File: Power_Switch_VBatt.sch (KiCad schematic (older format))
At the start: 11 parts

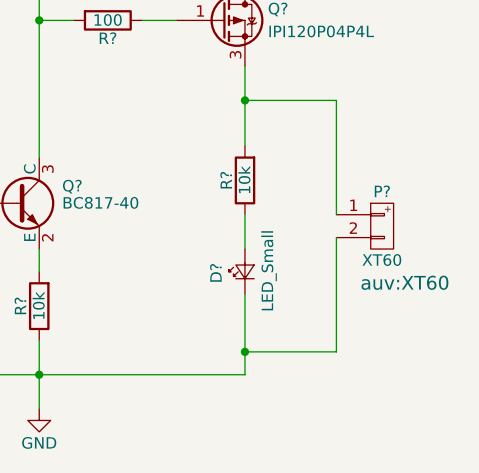
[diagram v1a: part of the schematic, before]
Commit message: Correct all foot-print assignments
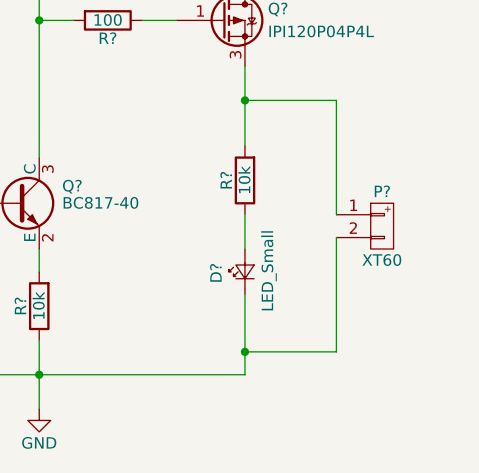
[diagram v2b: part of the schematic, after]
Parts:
- P?: footprint auv:XT60 -> zeabus:XT60
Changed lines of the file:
@@
 $Descr A4 11693 8268
 encoding utf-8
-Sheet 7 12
+Sheet 7 13
 Title ""
 Date ""
@@
 F 0 "P?" H 7050 4350 50  0000 C CNN
 F 1 "XT60" H 7050 4050 50  0000 C CNN
-F 2 "auv:XT60" H 7150 3950 60  0000 C CNN
+F 2 "zeabus:XT60" H 7150 3950 60  0001 C CNN
 F 3 "" H 7050 4200 60  0000 C CNN
 	1    7050 4200

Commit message: Annotate all components
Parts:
- gave numbers to parts that had none: 11
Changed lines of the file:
@@
 LIBS:zeabus
 LIBS:ftdi
-LIBS:Power_Distributor-cache
 EELAYER 25 0
 EELAYER END
 $Descr A4 11693 8268
 encoding utf-8
-Sheet 7 13
+Sheet 8 13
 Title ""
 Date ""
@@
 $EndDescr
 $Comp
-L Q_PMOS_GDS Q?
+L Q_PMOS_GDS Q6
 U 1 1 58E52089
 P 6350 3300
-AR Path="/58E527AF/58E52089" Ref="Q?"  Part="1"
-AR Path="/58E51F99/58E52089" Ref="Q?"  Part="1"
-F 0 "Q?" H 6550 3350 50  0000 L CNN
+AR Path="/58E51F99/58E52089" Ref="Q6"  Part="1"
+AR Path="/58E527AF/58E52089" Ref="Q8"  Part="1"
+F 0 "Q8" H 6550 3350 50  0000 L CNN
 F 1 "IPI120P04P4L" H 6550 3250 50  0000 L CNN
 F 2 "TO_SOT_Packages_SMD:TO-263-3Lead" H 6550 3400 50  0001 C CNN
@@
 $EndComp
 $Comp
-L R R?
+L R R16
 U 1 1 58E5219E
 P 5850 3300
-AR Path="/58E527AF/58E5219E" Ref="R?"  Part="1"
-AR Path="/58E51F99/58E5219E" Ref="R?"  Part="1"
-F 0 "R?" V 5930 3300 50  0000 C CNN
+AR Path="/58E51F99/58E5219E" Ref="R16"  Part="1"
+AR Path="/58E527AF/58E5219E" Ref="R21"  Part="1"
+F 0 "R21" V 5930 3300 50  0000 C CNN
 F 1 "100" V 5850 3300 50  0000 C CNN
 F 2 "Resistors_SMD:R_0603" V 5780 3300 50  0001 C CNN
@@
 $EndComp
 $Comp
-L XT60 P?
+L XT60 P12
 U 1 1 58E521F9
 P 7050 4200
-AR Path="/58E527AF/58E521F9" Ref="P?"  Part="1"
-AR Path="/58E51F99/58E521F9" Ref="P?"  Part="1"
-F 0 "P?" H 7050 4350 50  0000 C CNN
+AR Path="/58E51F99/58E521F9" Ref="P12"  Part="1"
+AR Path="/58E527AF/58E521F9" Ref="P13"  Part="1"
+F 0 "P13" H 7050 4350 50  0000 C CNN
 F 1 "XT60" H 7050 4050 50  0000 C CNN
 F 2 "zeabus:XT60" H 7150 3950 60  0001 C CNN
@@
 $EndComp
 $Comp
-L LED_Small D?
+L LED_Small D9
 U 1 1 58E52234
 P 6450 4400
-AR Path="/58E527AF/58E52234" Ref="D?"  Part="1"
-AR Path="/58E51F99/58E52234" Ref="D?"  Part="1"
-F 0 "D?" H 6400 4525 50  0000 L CNN
+AR Path="/58E51F99/58E52234" Ref="D9"  Part="1"
+AR Path="/58E527AF/58E52234" Ref="D11"  Part="1"
+F 0 "D11" H 6400 4525 50  0000 L CNN
 F 1 "LED_Small" H 6275 4300 50  0000 L CNN
 F 2 "LEDs:LED_0603" V 6450 4400 50  0001 C CNN
@@
 $EndComp
 $Comp
-L R R?
+L R R15
 U 1 1 58E5234D
 P 5850 2950
-AR Path="/58E527AF/58E5234D" Ref="R?"  Part="1"
-AR Path="/58E51F99/58E5234D" Ref="R?"  Part="1"
-F 0 "R?" V 5930 2950 50  0000 C CNN
+AR Path="/58E51F99/58E5234D" Ref="R15"  Part="1"
+AR Path="/58E527AF/58E5234D" Ref="R20"  Part="1"
+F 0 "R20" V 5930 2950 50  0000 C CNN
 F 1 "10k" V 5850 2950 50  0000 C CNN
 F 2 "Resistors_SMD:R_0603" V 5780 2950 50  0001 C CNN
@@
 $EndComp
 $Comp
-L R R?
+L R R17
 U 1 1 58E52389
 P 6450 4000
-AR Path="/58E527AF/58E52389" Ref="R?"  Part="1"
-AR Path="/58E51F99/58E52389" Ref="R?"  Part="1"
-F 0 "R?" V 6530 4000 50  0000 C CNN
+AR Path="/58E51F99/58E52389" Ref="R17"  Part="1"
+AR Path="/58E527AF/58E52389" Ref="R22"  Part="1"
+F 0 "R22" V 6530 4000 50  0000 C CNN
 F 1 "10k" V 6450 4000 50  0000 C CNN
 F 2 "Resistors_SMD:R_0603" V 6380 4000 50  0001 C CNN
@@
 $EndComp
 $Comp
-L BC817-40 Q?
+L BC817-40 Q5
 U 1 1 58E52473
 P 5450 4100
-AR Path="/58E527AF/58E52473" Ref="Q?"  Part="1"
-AR Path="/58E51F99/58E52473" Ref="Q?"  Part="1"
-F 0 "Q?" H 5650 4175 50  0000 L CNN
+AR Path="/58E51F99/58E52473" Ref="Q5"  Part="1"
+AR Path="/58E527AF/58E52473" Ref="Q7"  Part="1"
+F 0 "Q7" H 5650 4175 50  0000 L CNN
 F 1 "BC817-40" H 5650 4100 50  0000 L CNN
 F 2 "TO_SOT_Packages_SMD:SOT-23" H 5650 4025 50  0001 L CIN
@@
 $EndComp
 $Comp
-L R R?
+L R R13
 U 1 1 58E526E2
 P 4300 4100
-AR Path="/58E527AF/58E526E2" Ref="R?"  Part="1"
-AR Path="/58E51F99/58E526E2" Ref="R?"  Part="1"
-F 0 "R?" V 4380 4100 50  0000 C CNN
+AR Path="/58E51F99/58E526E2" Ref="R13"  Part="1"
+AR Path="/58E527AF/58E526E2" Ref="R18"  Part="1"
+F 0 "R18" V 4380 4100 50  0000 C CNN
 F 1 "2.2k" V 4300 4100 50  0000 C CNN
 F 2 "Resistors_SMD:R_0603" V 4230 4100 50  0001 C CNN
@@
 $EndComp
 $Comp
-L C C?
+L C C2
 U 1 1 58E5272C
 P 4900 4400
-AR Path="/58E527AF/58E5272C" Ref="C?"  Part="1"
-AR Path="/58E51F99/58E5272C" Ref="C?"  Part="1"
-F 0 "C?" H 4925 4500 50  0000 L CNN
+AR Path="/58E51F99/58E5272C" Ref="C2"  Part="1"
+AR Path="/58E527AF/58E5272C" Ref="C3"  Part="1"
+F 0 "C3" H 4925 4500 50  0000 L CNN
 F 1 "1nF" H 4925 4300 50  0000 L CNN
 F 2 "Capacitors_SMD:C_0603" H 4938 4250 50  0001 C CNN
@@
 $EndComp
 $Comp
-L D D?
+L D D8
 U 1 1 58E5279D
 P 4600 4400
-AR Path="/58E527AF/58E5279D" Ref="D?"  Part="1"
-AR Path="/58E51F99/58E5279D" Ref="D?"  Part="1"
-F 0 "D?" H 4600 4500 50  0000 C CNN
+AR Path="/58E51F99/58E5279D" Ref="D8"  Part="1"
+AR Path="/58E527AF/58E5279D" Ref="D10"  Part="1"
+F 0 "D10" H 4600 4500 50  0000 C CNN
 F 1 "D" H 4600 4300 50  0000 C CNN
 F 2 "Diodes_SMD:D_SOD-123" H 4600 4400 50  0001 C CNN
@@
 $EndComp
 $Comp
-L GND #PWR?
+L GND #PWR021
 U 1 1 58E527F8
 P 5550 5000
-AR Path="/58E527AF/58E527F8" Ref="#PWR?"  Part="1"
-AR Path="/58E51F99/58E527F8" Ref="#PWR?"  Part="1"
-F 0 "#PWR?" H 5550 4750 50  0001 C CNN
+AR Path="/58E51F99/58E527F8" Ref="#PWR021"  Part="1"
+AR Path="/58E527AF/58E527F8" Ref="#PWR022"  Part="1"
+F 0 "#PWR022" H 5550 4750 50  0001 C CNN
 F 1 "GND" H 5550 4850 50  0000 C CNN
 F 2 "" H 5550 5000 50  0001 C CNN
@@
 	6850 4250 6850 4750
 $Comp
-L R R?
+L R R14
 U 1 1 58E6A1DE
 P 5550 4550
-AR Path="/58E51F99/58E6A1DE" Ref="R?"  Part="1"
-AR Path="/58E527AF/58E6A1DE" Ref="R?"  Part="1"
-F 0 "R?" V 5630 4550 50  0000 C CNN
+AR Path="/58E51F99/58E6A1DE" Ref="R14"  Part="1"
+AR Path="/58E527AF/58E6A1DE" Ref="R19"  Part="1"
+F 0 "R19" V 5630 4550 50  0000 C CNN
 F 1 "10k" V 5550 4550 50  0000 C CNN
 F 2 "Resistors_SMD:R_0603" V 5480 4550 50  0001 C CNN

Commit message: Bug fixed and clean-up for PCB generating
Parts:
- removed D8: D, Diodes_SMD:D_SOD-123, symbol D
- added D4: BZX585-C12, Diodes_SMD:SOD-523, symbol D_Zener
- added F2: Fuse, Zeabus:FUSE_AUTO, symbol Fuse
- C2: value 1nF -> 1uF
- Q4: renamed from Q6; value IPI120P04P4L -> IPD90P03P4L; footprint TO_SOT_Packages_SMD:TO-263-3Lead -> TO_SOT_Packages_SMD:TO-252-2Lead
- R9: renamed from R16; value 100 -> 1k
- renumbered D9 to D5, P12 to P5, Q5 to Q3, R17 to R10, R13 to R6, R14 to R7, R15 to R8
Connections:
- net labels removed: Hardware_Switch
- wire segments 24 -> 23
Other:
- moved on the sheet: D7, P6, R13, R15
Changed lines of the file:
@@
 $Descr A4 11693 8268
 encoding utf-8
-Sheet 8 13
+Sheet 3 10
 Title ""
-Date ""
-Rev ""
+Date "2017-04-06"
+Rev "1.0.0"
 Comp ""
 Comment1 ""
@@
 $EndDescr
 $Comp
-L Q_PMOS_GDS Q6
+L Q_PMOS_GDS Q4
 U 1 1 58E52089
 P 6350 3300
-AR Path="/58E51F99/58E52089" Ref="Q6"  Part="1"
-AR Path="/58E527AF/58E52089" Ref="Q8"  Part="1"
-F 0 "Q8" H 6550 3350 50  0000 L CNN
-F 1 "IPI120P04P4L" H 6550 3250 50  0000 L CNN
-F 2 "TO_SOT_Packages_SMD:TO-263-3Lead" H 6550 3400 50  0001 C CNN
+AR Path="/58E51F99/58E52089" Ref="Q4"  Part="1"
+AR Path="/58E527AF/58E52089" Ref="Q6"  Part="1"
+F 0 "Q6" H 6550 3350 50  0000 L CNN
+F 1 "IPD90P03P4L" H 6550 3250 50  0000 L CNN
+F 2 "TO_SOT_Packages_SMD:TO-252-2Lead" H 6550 3400 50  0001 C CNN
 F 3 "" H 6350 3300 50  0001 C CNN
 	1    6350 3300
@@
 $EndComp
 $Comp
-L R R16
+L R R9
 U 1 1 58E5219E
 P 5850 3300
-AR Path="/58E51F99/58E5219E" Ref="R16"  Part="1"
-AR Path="/58E527AF/58E5219E" Ref="R21"  Part="1"
-F 0 "R21" V 5930 3300 50  0000 C CNN
-F 1 "100" V 5850 3300 50  0000 C CNN
+AR Path="/58E51F99/58E5219E" Ref="R9"  Part="1"
+AR Path="/58E527AF/58E5219E" Ref="R14"  Part="1"
+F 0 "R14" V 5930 3300 50  0000 C CNN
+F 1 "1k" V 5850 3300 50  0000 C CNN
 F 2 "Resistors_SMD:R_0603" V 5780 3300 50  0001 C CNN
 F 3 "" H 5850 3300 50  0001 C CNN
@@
 $EndComp
 $Comp
-L XT60 P12
+L XT60 P5
 U 1 1 58E521F9
-P 7050 4200
-AR Path="/58E51F99/58E521F9" Ref="P12"  Part="1"
-AR Path="/58E527AF/58E521F9" Ref="P13"  Part="1"
-F 0 "P13" H 7050 4350 50  0000 C CNN
-F 1 "XT60" H 7050 4050 50  0000 C CNN
-F 2 "zeabus:XT60" H 7150 3950 60  0001 C CNN
-F 3 "" H 7050 4200 60  0000 C CNN
-	1    7050 4200
-	1    0    0    -1
-$EndComp
-$Comp
-L LED_Small D9
+P 7050 4250
+AR Path="/58E51F99/58E521F9" Ref="P5"  Part="1"
+AR Path="/58E527AF/58E521F9" Ref="P6"  Part="1"
+F 0 "P6" H 7050 4400 50  0000 C CNN
+F 1 "XT60" H 7050 4100 50  0000 C CNN
+F 2 "zeabus:XT60" H 7150 4000 60  0001 C CNN
+F 3 "" H 7050 4250 60  0000 C CNN
+	1    7050 4250
+	1    0    0    -1
+$EndComp
+$Comp
+L LED_Small D5
 U 1 1 58E52234
-P 6450 4400
-AR Path="/58E51F99/58E52234" Ref="D9"  Part="1"
-AR Path="/58E527AF/58E52234" Ref="D11"  Part="1"
-F 0 "D11" H 6400 4525 50  0000 L CNN
-F 1 "LED_Small" H 6275 4300 50  0000 L CNN
-F 2 "LEDs:LED_0603" V 6450 4400 50  0001 C CNN
-F 3 "" V 6450 4400 50  0001 C CNN
-	1    6450 4400
+P 6450 4550
+AR Path="/58E51F99/58E52234" Ref="D5"  Part="1"
+AR Path="/58E527AF/58E52234" Ref="D7"  Part="1"
+F 0 "D7" H 6400 4675 50  0000 L CNN
+F 1 "LED_Small" H 6275 4450 50  0000 L CNN
+F 2 "LEDs:LED_0603" V 6450 4550 50  0001 C CNN
+F 3 "" V 6450 4550 50  0001 C CNN
+	1    6450 4550
 	0    -1   -1   0
 $EndComp
 $Comp
-L R R15
+L R R8
 U 1 1 58E5234D
-P 5850 2950
-AR Path="/58E51F99/58E5234D" Ref="R15"  Part="1"
-AR Path="/58E527AF/58E5234D" Ref="R20"  Part="1"
-F 0 "R20" V 5930 2950 50  0000 C CNN
-F 1 "10k" V 5850 2950 50  0000 C CNN
-F 2 "Resistors_SMD:R_0603" V 5780 2950 50  0001 C CNN
-F 3 "" H 5850 2950 50  0001 C CNN
-	1    5850 2950
-	0    1    1    0
-$EndComp
-$Comp
-L R R17
+P 5850 2700
+AR Path="/58E51F99/58E5234D" Ref="R8"  Part="1"
+AR Path="/58E527AF/58E5234D" Ref="R13"  Part="1"
+F 0 "R13" V 5930 2700 50  0000 C CNN
+F 1 "10k" V 5850 2700 50  0000 C CNN
+F 2 "Resistors_SMD:R_0603" V 5780 2700 50  0001 C CNN
+F 3 "" H 5850 2700 50  0001 C CNN
+	1    5850 2700
+	0    1    1    0
+$EndComp
+$Comp
+L R R10
 U 1 1 58E52389
-P 6450 4000
-AR Path="/58E51F99/58E52389" Ref="R17"  Part="1"
-AR Path="/58E527AF/58E52389" Ref="R22"  Part="1"
-F 0 "R22" V 6530 4000 50  0000 C CNN
-F 1 "10k" V 6450 4000 50  0000 C CNN
-F 2 "Resistors_SMD:R_0603" V 6380 4000 50  0001 C CNN
-F 3 "" H 6450 4000 50  0001 C CNN
-	1    6450 4000
+P 6450 4150
+AR Path="/58E51F99/58E52389" Ref="R10"  Part="1"
+AR Path="/58E527AF/58E52389" Ref="R15"  Part="1"
+F 0 "R15" V 6530 4150 50  0000 C CNN
+F 1 "10k" V 6450 4150 50  0000 C CNN
+F 2 "Resistors_SMD:R_0603" V 6380 4150 50  0001 C CNN
+F 3 "" H 6450 4150 50  0001 C CNN
+	1    6450 4150
 	-1   0    0    1
 $EndComp
 $Comp
-L BC817-40 Q5
+L BC817-40 Q3
 U 1 1 58E52473
 P 5450 4100
-AR Path="/58E51F99/58E52473" Ref="Q5"  Part="1"
-AR Path="/58E527AF/58E52473" Ref="Q7"  Part="1"
-F 0 "Q7" H 5650 4175 50  0000 L CNN
+AR Path="/58E51F99/58E52473" Ref="Q3"  Part="1"
+AR Path="/58E527AF/58E52473" Ref="Q5"  Part="1"
+F 0 "Q5" H 5650 4175 50  0000 L CNN
 F 1 "BC817-40" H 5650 4100 50  0000 L CNN
 F 2 "TO_SOT_Packages_SMD:SOT-23" H 5650 4025 50  0001 L CIN
@@
 $EndComp
 $Comp
-L R R13
+L R R6
 U 1 1 58E526E2
 P 4300 4100
-AR Path="/58E51F99/58E526E2" Ref="R13"  Part="1"
-AR Path="/58E527AF/58E526E2" Ref="R18"  Part="1"
-F 0 "R18" V 4380 4100 50  0000 C CNN
+AR Path="/58E51F99/58E526E2" Ref="R6"  Part="1"
+AR Path="/58E527AF/58E526E2" Ref="R11"  Part="1"
+F 0 "R11" V 4380 4100 50  0000 C CNN
 F 1 "2.2k" V 4300 4100 50  0000 C CNN
 F 2 "Resistors_SMD:R_0603" V 4230 4100 50  0001 C CNN
@@
 AR Path="/58E527AF/58E5272C" Ref="C3"  Part="1"
 F 0 "C3" H 4925 4500 50  0000 L CNN
-F 1 "1nF" H 4925 4300 50  0000 L CNN
+F 1 "1uF" H 4925 4300 50  0000 L CNN
 F 2 "Capacitors_SMD:C_0603" H 4938 4250 50  0001 C CNN
 F 3 "" H 4900 4400 50  0001 C CNN
@@
 $EndComp
 $Comp
-L D D8
-U 1 1 58E5279D
-P 4600 4400
-AR Path="/58E51F99/58E5279D" Ref="D8"  Part="1"
-AR Path="/58E527AF/58E5279D" Ref="D10"  Part="1"
-F 0 "D10" H 4600 4500 50  0000 C CNN
-F 1 "D" H 4600 4300 50  0000 C CNN
-F 2 "Diodes_SMD:D_SOD-123" H 4600 4400 50  0001 C CNN
-F 3 "" H 4600 4400 50  0001 C CNN
-	1    4600 4400
-	0    -1   -1   0
-$EndComp
-$Comp
-L GND #PWR021
+L GND #PWR17
 U 1 1 58E527F8
 P 5550 5000
-AR Path="/58E51F99/58E527F8" Ref="#PWR021"  Part="1"
-AR Path="/58E527AF/58E527F8" Ref="#PWR022"  Part="1"
-F 0 "#PWR022" H 5550 4750 50  0001 C CNN
+AR Path="/58E51F99/58E527F8" Ref="#PWR17"  Part="1"
+AR Path="/58E527AF/58E527F8" Ref="#PWR18"  Part="1"
+F 0 "#PWR18" H 5550 4750 50  0001 C CNN
 F 1 "GND" H 5550 4850 50  0000 C CNN
 F 2 "" H 5550 5000 50  0001 C CNN
@@
 	1    0    0    -1
 $EndComp
-Text HLabel 3650 2750 0    60   Input ~ 0
+Text HLabel 3650 2450 0    60   Input ~ 0
 +Power
 Text HLabel 3650 4100 0    60   Input ~ 0
 Software_Switch
-Text HLabel 3650 4650 0    60   Input ~ 0
-Hardware_Switch
-Wire Wire Line
-	6450 3500 6450 3850
-Wire Wire Line
-	6450 3650 6850 3650
-Connection ~ 6450 3650
 Wire Wire Line
 	6000 3300 6150 3300
 Wire Wire Line
-	5550 2950 5700 2950
-Wire Wire Line
 	5550 3300 5700 3300
 Wire Wire Line
-	5550 2950 5550 3900
+	5550 2700 5550 3900
 Connection ~ 5550 3300
 Wire Wire Line
@@
 	4900 4550 4900 4850
 Connection ~ 4900 4100
-Connection ~ 4600 4100
 Wire Wire Line
 	3650 4100 4150 4100
 Wire Wire Line
-	6450 2750 6450 3100
-Wire Wire Line
-	6450 2950 6000 2950
-Connection ~ 6450 2950
-Wire Wire Line
-	4600 4100 4600 4250
-Wire Wire Line
-	4600 4550 4600 4650
-Wire Wire Line
-	4600 4650 3650 4650
-Wire Wire Line
-	6450 4150 6450 4300
-Wire Wire Line
-	6450 4850 6450 4500
-Wire Wire Line
-	6850 3650 6850 4150
-Wire Wire Line
-	6850 4250 6850 4750
-$Comp
-L R R14
+	6450 2450 6450 3100
+$Comp
+L R R7
 U 1 1 58E6A1DE
 P 5550 4550
-AR Path="/58E51F99/58E6A1DE" Ref="R14"  Part="1"
-AR Path="/58E527AF/58E6A1DE" Ref="R19"  Part="1"
-F 0 "R19" V 5630 4550 50  0000 C CNN
+AR Path="/58E51F99/58E6A1DE" Ref="R7"  Part="1"
+AR Path="/58E527AF/58E6A1DE" Ref="R12"  Part="1"
+F 0 "R12" V 5630 4550 50  0000 C CNN
 F 1 "10k" V 5550 4550 50  0000 C CNN
 F 2 "Resistors_SMD:R_0603" V 5480 4550 50  0001 C CNN
@@
 	-1   0    0    1
 $EndComp
-Wire Wire Line
-	6850 4750 6450 4750
 Connection ~ 5550 4850
-Connection ~ 6450 4750
-Wire Wire Line
-	3650 2750 6450 2750
-Wire Wire Line
-	4900 4850 6450 4850
+Wire Wire Line
+	4900 4850 6850 4850
 Wire Wire Line
 	5550 4300 5550 4400
 Wire Wire Line
 	5550 4700 5550 5000
+$Comp
+L D_Zener D4
+U 1 1 58E648CE
+P 6100 3000
+AR Path="/58E51F99/58E648CE" Ref="D4"  Part="1"
+AR Path="/58E527AF/58E648CE" Ref="D6"  Part="1"
+F 0 "D6" H 6100 3100 50  0000 C CNN
+F 1 "BZX585-C12" H 6100 2900 50  0000 C CNN
+F 2 "Diodes_SMD:SOD-523" H 6100 3000 50  0001 C CNN
+F 3 "" H 6100 3000 50  0001 C CNN
+	1    6100 3000
+	0    1    1    0
+$EndComp
+Wire Wire Line
+	5550 2700 5700 2700
+Wire Wire Line
+	6000 2700 6450 2700
+Wire Wire Line
+	6100 2850 6100 2700
+Connection ~ 6100 2700
+Wire Wire Line
+	6100 3150 6100 3300
+Connection ~ 6100 3300
+Wire Wire Line
+	3650 2450 6450 2450
+Connection ~ 6450 2700
+$Comp
+L Fuse F2
+U 1 1 58E651FD
+P 6450 3750
+AR Path="/58E51F99/58E651FD" Ref="F2"  Part="1"
+AR Path="/58E527AF/58E651FD" Ref="F3"  Part="1"
+F 0 "F3" V 6530 3750 50  0000 C CNN
+F 1 "Fuse" V 6375 3750 50  0000 C CNN
+F 2 "Zeabus:FUSE_AUTO" V 6380 3750 50  0001 C CNN
+F 3 "" H 6450 3750 50  0001 C CNN
+	1    6450 3750
+	1    0    0    -1
+$EndComp
+Wire Wire Line
+	6450 3500 6450 3600
+Wire Wire Line
+	6450 3900 6450 4000
+Wire Wire Line
+	6450 4300 6450 4450
+Wire Wire Line
+	6450 4850 6450 4650
+Wire Wire Line
+	6850 4850 6850 4300
+Connection ~ 6450 4850
+Wire Wire Line
+	6450 3950 6850 3950
+Wire Wire Line
+	6850 3950 6850 4200
+Connection ~ 6450 3950
 $EndSCHEMATC
